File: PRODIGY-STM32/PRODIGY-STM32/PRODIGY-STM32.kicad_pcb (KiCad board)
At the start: 2 copper layers, 55 x 40 mm, 9 parts, among them J1 DF40C-100DS-0.4V(51), J2 DF40C-100DS-0.4V(51), Q1 BC850, U1 STM32F103C8Tx, U2 STM32U5F9ZJTxQ

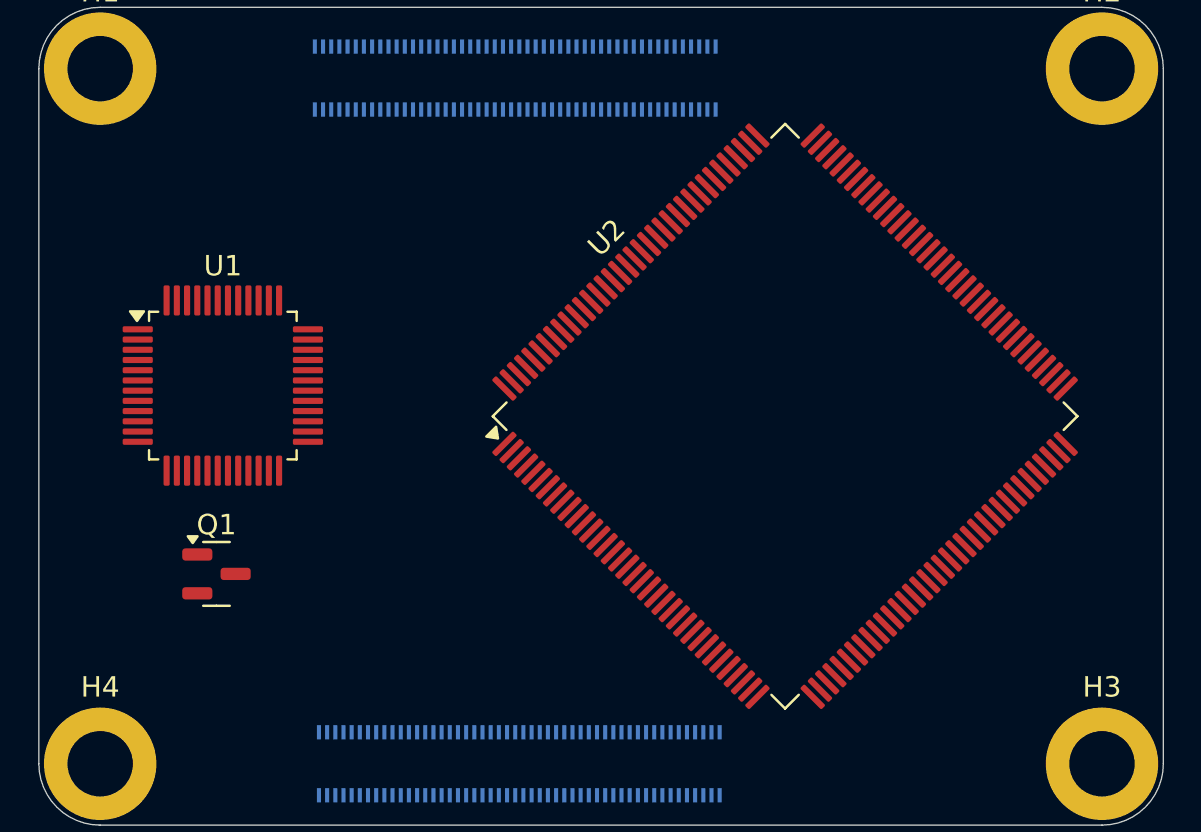
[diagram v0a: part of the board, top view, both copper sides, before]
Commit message: stm32 schematic finished
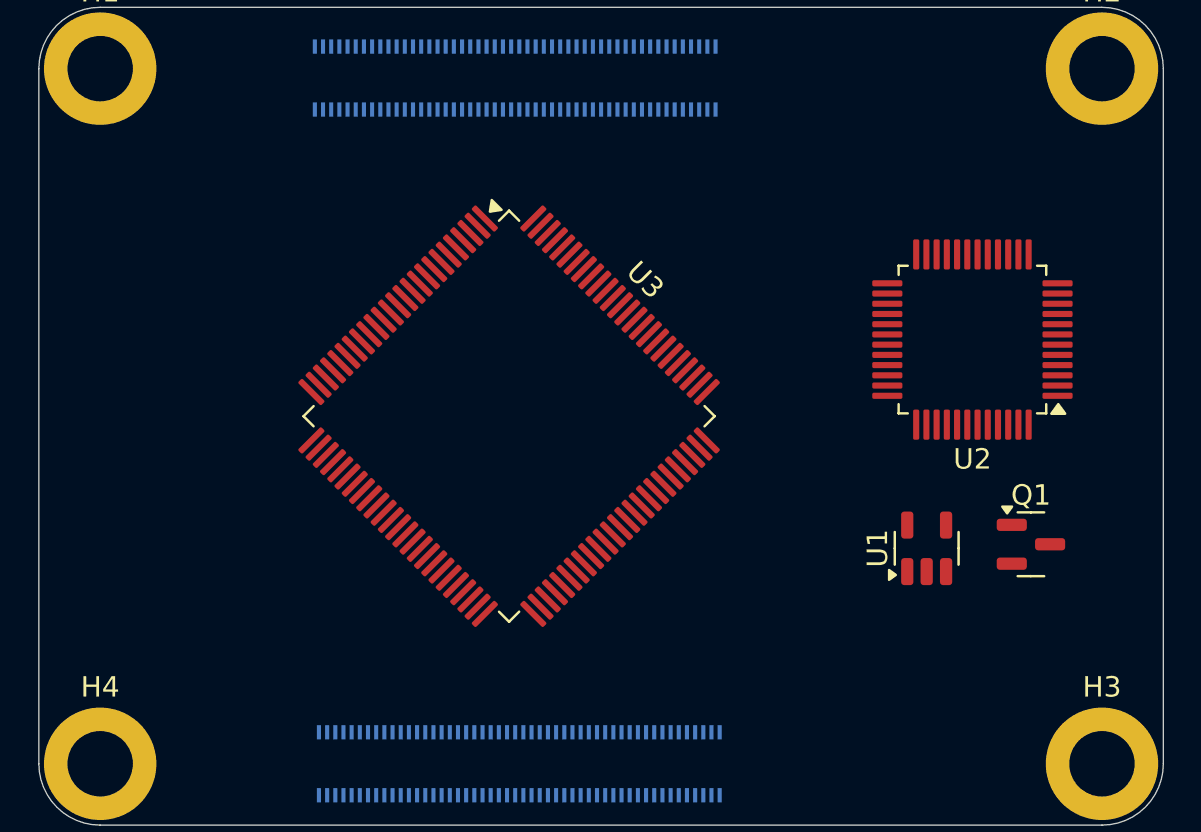
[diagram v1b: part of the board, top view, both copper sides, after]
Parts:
- added U3: STM32F407VGTx, Package_QFP:LQFP-100_14x14mm_P0.5mm, F.Cu at (123.0, 75.0)
- U1: value STM32F103C8Tx -> AP2112K-3.3; footprint Package_QFP:LQFP-48_7x7mm_P0.5mm -> Package_TO_SOT_SMD:SOT-23-5
- U2: value STM32U5F9ZJTxQ -> STM32F103C8Tx; footprint Package_QFP:LQFP-144_20x20mm_P0.5mm -> Package_QFP:LQFP-48_7x7mm_P0.5mm
- moved Q1 39.9 mm to (148.5, 81.3)
- moved U1 35.3 mm to (143.4, 81.5), turned to 90 degrees
- moved U2 9.90 mm to (145.7, 71.2), turned to 180 degrees
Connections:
- J1 pad 5: /Connector-1/USB_DP+ -> /st-link-v2/USB_D+
- U1 pad 1: +3V3 -> +5V
- U1 pad 2: Net-(U1-PC13) -> GND
- U1 pad 3: Net-(U1-PC14) -> +5V
- U1 pad 5: Net-(U1-PD0) -> +3V3
- U2 pad 1: unconnected-(U2-PE2-Pad1) -> +3V3
- U2 pad 10: unconnected-(U2-PF0-Pad10) -> Net-(U2-PA0)
- U2 pad 12: unconnected-(U2-PF2-Pad12) -> /mcu/T_TX
- U2 pad 13: +3V3 -> /mcu/T_RX
- U2 pad 14: +3V3 -> unconnected-(U2-PA4-Pad14)
- U2 pad 15: unconnected-(U2-DSI_D0P-Pad15) -> /st-link-v2/CLK
- U2 pad 17: GND -> unconnected-(U2-PA7-Pad17)
- U2 pad 18: unconnected-(U2-DSI_CKP-Pad18) -> /mcu/T_RST
- U2 pad 2: unconnected-(U2-PE3-Pad2) -> Net-(U2-PC13)
- U2 pad 20: +3V3 -> unconnected-(U2-PB2-Pad20)
- U2 pad 24: GND -> +3V3
- U2 pad 25: +3V3 -> Net-(U2-PB12)
- U2 pad 26: unconnected-(U2-PH0-Pad26) -> /st-link-v2/CLK
- U2 pad 27: unconnected-(U2-PH1-Pad27) -> /mcu/T_DIO
- U2 pad 3: unconnected-(U2-PE4-Pad3) -> Net-(U2-PC14)
- U2 pad 30: unconnected-(U2-PC1-Pad30) -> /st-link-v2/LED
- U2 pad 31: unconnected-(U2-PC2-Pad31) -> /mcu/T_SWO
- U2 pad 32: unconnected-(U2-PC3-Pad32) -> /Connector-1/USB_DP-
- U2 pad 33: GND -> /st-link-v2/USB_D+
- U2 pad 34: unconnected-(U2-VREF+-Pad34) -> /st-link-v2/DIO
- U2 pad 35: +3V3 -> GND
- U2 pad 36: unconnected-(U2-PA0-Pad36) -> +3V3
- U2 pad 37: unconnected-(U2-PA1-Pad37) -> /st-link-v2/CLK
- U2 pad 38: unconnected-(U2-PA2-Pad38) -> /st-link-v2/RENUM
- U2 pad 40: GND -> unconnected-(U2-PB4-Pad40)
- U2 pad 41: +3V3 -> unconnected-(U2-PB5-Pad41)
- U2 pad 44: unconnected-(U2-PA6-Pad44) -> /mcu/BOOT
- U2 pad 47: unconnected-(U2-PB1-Pad47) -> GND
- U2 pad 48: unconnected-(U2-PB2-Pad48) -> +3V3
- U2 pad 5: unconnected-(U2-PE6-Pad5) -> Net-(U2-PD0)
- U2 pad 6: +3V3 -> Net-(U2-PD1)
- U2 pad 7: unconnected-(U2-PC13-Pad7) -> /st-link-v2/RESET
- U2 pad 8: unconnected-(U2-PC14-Pad8) -> GND
- U2 pad 9: unconnected-(U2-PC15-Pad9) -> +3V3

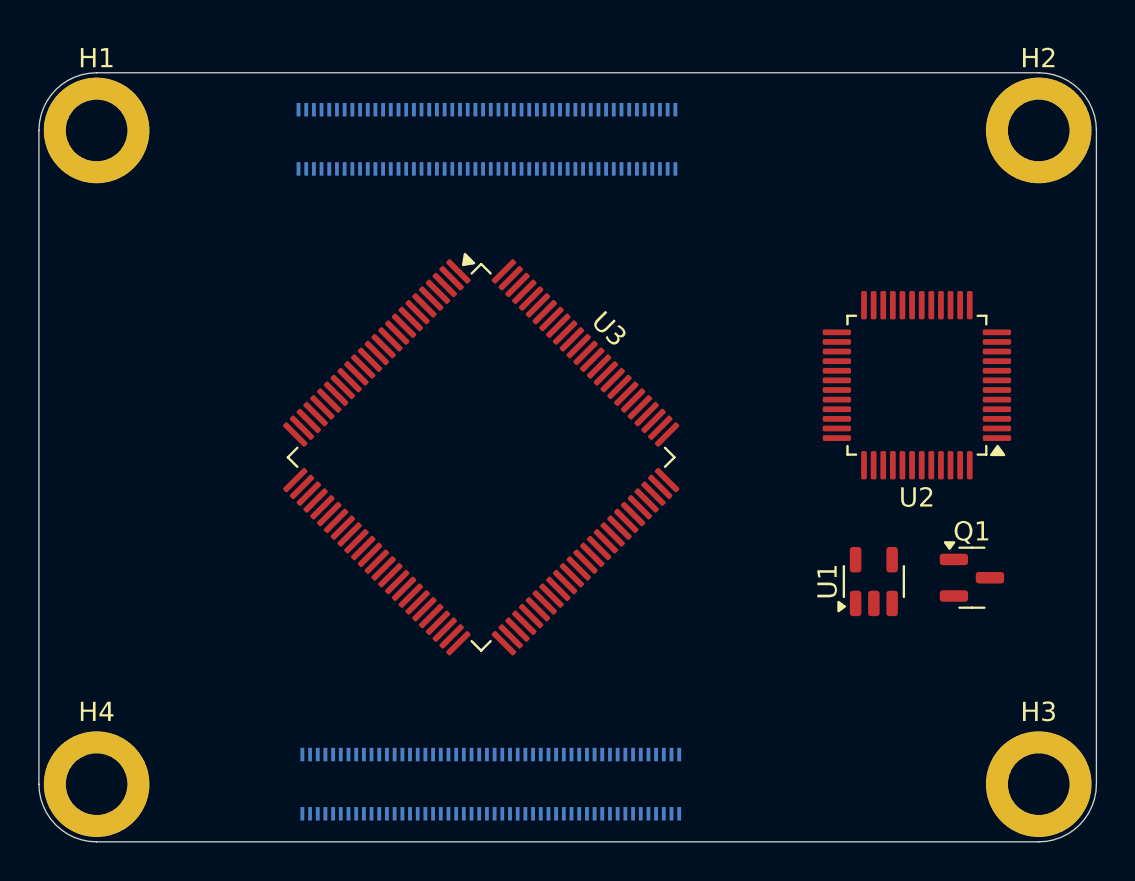
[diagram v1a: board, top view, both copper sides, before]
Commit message: All footprint assosiations have been made across all schematics.
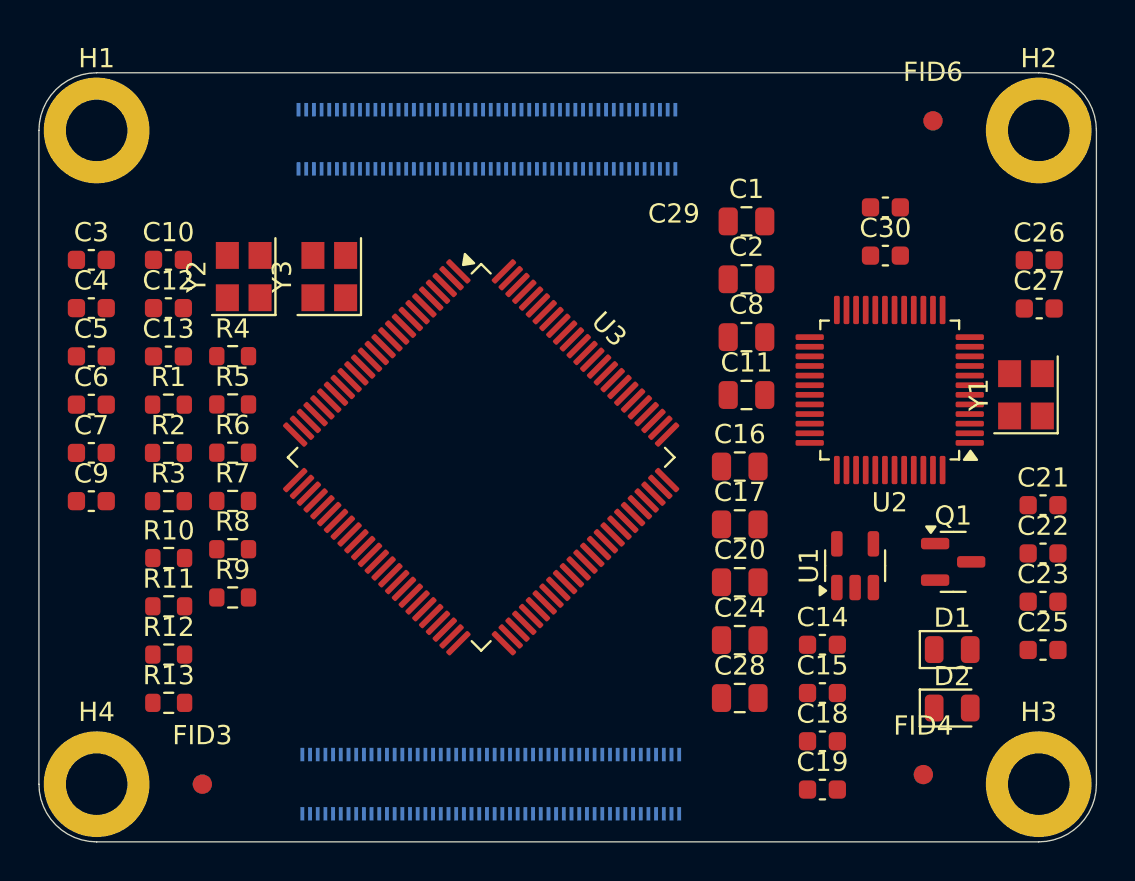
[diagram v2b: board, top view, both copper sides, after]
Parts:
- added C1: 10uF, Capacitor_SMD:C_0805_2012Metric, F.Cu at (136.8, 62.7)
- added C10: 100nF, Capacitor_SMD:C_0603_1608Metric, F.Cu at (106.7, 64.7)
- added C11: 10uF, Capacitor_SMD:C_0805_2012Metric, F.Cu at (136.8, 71.8)
- added C12: 100nF, Capacitor_SMD:C_0603_1608Metric, F.Cu at (106.7, 67.2)
- added C13: 100nF, Capacitor_SMD:C_0603_1608Metric, F.Cu at (106.7, 69.8)
- added C14: 4.7pF, Capacitor_SMD:C_0603_1608Metric, F.Cu at (140.8, 84.8)
- added C15: 4.7pF, Capacitor_SMD:C_0603_1608Metric, F.Cu at (140.8, 87.3)
- added C16: 2.2uF, Capacitor_SMD:C_0805_2012Metric, F.Cu at (136.4, 75.5)
- added C17: 2.2uF, Capacitor_SMD:C_0805_2012Metric, F.Cu at (136.4, 78.5)
- added C18: 2.7pF, Capacitor_SMD:C_0603_1608Metric, F.Cu at (140.8, 89.8)
- added C19: 2.7pF, Capacitor_SMD:C_0603_1608Metric, F.Cu at (140.8, 92.3)
- added C2: 10uF, Capacitor_SMD:C_0805_2012Metric, F.Cu at (136.8, 65.7)
- added C20: 10uF, Capacitor_SMD:C_0805_2012Metric, F.Cu at (136.4, 81.5)
- added C21: 100nF, Capacitor_SMD:C_0603_1608Metric, F.Cu at (152.2, 77.5)
- added C22: 100nF, Capacitor_SMD:C_0603_1608Metric, F.Cu at (152.2, 80.0)
- added C23: 100nF, Capacitor_SMD:C_0603_1608Metric, F.Cu at (152.2, 82.5)
- added C24: 10uF, Capacitor_SMD:C_0805_2012Metric, F.Cu at (136.4, 84.5)
- added C25: 100nF, Capacitor_SMD:C_0603_1608Metric, F.Cu at (152.2, 85.0)
- added C26: 100nF, Capacitor_SMD:C_0603_1608Metric, F.Cu at (152.0, 64.8)
- added C27: 100nF, Capacitor_SMD:C_0603_1608Metric, F.Cu at (152.0, 67.3)
- added C28: 10uF, Capacitor_SMD:C_0805_2012Metric, F.Cu at (136.4, 87.5)
- added C29: 100nF, Capacitor_SMD:C_0603_1608Metric, F.Cu at (144.0, 62.0)
- added C3: 100nF, Capacitor_SMD:C_0603_1608Metric, F.Cu at (102.7, 64.7)
- added C30: 100nF, Capacitor_SMD:C_0603_1608Metric, F.Cu at (144.0, 64.5)
- added C4: 100nF, Capacitor_SMD:C_0603_1608Metric, F.Cu at (102.7, 67.2)
- added C5: 100nF, Capacitor_SMD:C_0603_1608Metric, F.Cu at (102.7, 69.8)
- added C6: 10pF, Capacitor_SMD:C_0603_1608Metric, F.Cu at (102.7, 72.3)
- added C7: 100nF, Capacitor_SMD:C_0603_1608Metric, F.Cu at (102.7, 74.8)
- added C8: 10uF, Capacitor_SMD:C_0805_2012Metric, F.Cu at (136.8, 68.8)
- added C9: 10pF, Capacitor_SMD:C_0603_1608Metric, F.Cu at (102.7, 77.3)
- added D1: LED, LED_SMD:LED_0805_2012Metric, F.Cu at (147.5, 85.0)
- added D2: LED, LED_SMD:LED_0805_2012Metric, F.Cu at (147.5, 88.0)
- added FID1: Fiducial, Fiducial:Fiducial_1mm_Mask3mm, B.Cu at (146.5, 57.5)
- added FID2: Fiducial, Fiducial:Fiducial_1mm_Mask3mm, B.Cu at (146.0, 91.5)
- added FID3: Fiducial, Fiducial:Fiducial_1mm_Mask3mm, F.Cu at (108.5, 92.0)
- added FID4: Fiducial, Fiducial:Fiducial_1mm_Mask3mm, F.Cu at (146.0, 91.5)
- added FID5: Fiducial, Fiducial:Fiducial_1mm_Mask3mm, B.Cu at (108.5, 92.0)
- added FID6: Fiducial, Fiducial:Fiducial_1mm_Mask3mm, F.Cu at (146.5, 57.5)
- added R1: 100k, Resistor_SMD:R_0603_1608Metric, F.Cu at (106.7, 72.3)
- added R10: 10k, Resistor_SMD:R_0603_1608Metric, F.Cu at (106.8, 80.2)
- added R11: 100, Resistor_SMD:R_0603_1608Metric, F.Cu at (106.8, 82.8)
- added R12: 1k, Resistor_SMD:R_0603_1608Metric, F.Cu at (106.8, 85.3)
- added R13: 1k, Resistor_SMD:R_0603_1608Metric, F.Cu at (106.8, 87.8)
- added R2: 10k, Resistor_SMD:R_0603_1608Metric, F.Cu at (106.7, 74.8)
- added R3: DNP, Resistor_SMD:R_0603_1608Metric, F.Cu at (106.7, 77.3)
- added R4: 100, Resistor_SMD:R_0603_1608Metric, F.Cu at (110.1, 69.7)
- added R5: 4k7, Resistor_SMD:R_0603_1608Metric, F.Cu at (110.1, 72.2)
- added R6: 4k7, Resistor_SMD:R_0603_1608Metric, F.Cu at (110.1, 74.8)
- added R7: 100k, Resistor_SMD:R_0603_1608Metric, F.Cu at (110.1, 77.3)
- added R8: 1k5, Resistor_SMD:R_0603_1608Metric, F.Cu at (110.1, 79.8)
- added R9: 10k, Resistor_SMD:R_0603_1608Metric, F.Cu at (110.1, 82.3)
- added Y1: 8MHz, Crystal:Crystal_SMD_3225-4Pin_3.2x2.5mm, F.Cu at (151.3, 71.8)
- added Y2: 8MHz, Crystal:Crystal_SMD_3225-4Pin_3.2x2.5mm, F.Cu at (110.7, 65.6)
- added Y3: 32.768kHz, Crystal:Crystal_SMD_3225-4Pin_3.2x2.5mm, F.Cu at (115.1, 65.6)
- moved U2 1.43 mm to (144.2, 71.5)
- moved U1 1.28 mm to (142.4, 80.6)
- moved Q1 1.28 mm to (147.6, 80.4)
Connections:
- J2 pad 88: +1V8 -> +3V3
- J2 pad 90: +1V8 -> +3V3

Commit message: STM32 bom done.
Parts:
- J1, J2: value DF40C-100DS-0.4V(51) -> DF40C-100DP-04V-51
- Y1, Y2: footprint Crystal:Crystal_SMD_3225-4Pin_3.2x2.5mm -> Crystal:Crystal_SMD_5032-4Pin_5.0x3.2mm
- Y3: footprint Crystal:Crystal_SMD_3225-4Pin_3.2x2.5mm -> Crystal:Crystal_SMD_MicroCrystal_CC7V-T1A-2Pin_3.2x1.5mm
- moved Y1 0.41 mm to (151.8, 71.8)
